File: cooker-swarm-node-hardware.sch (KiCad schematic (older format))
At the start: 18 parts, among them J2 Conn_INPUT, J3 Conn_OUTPUT, Q1 BSS138, Q2 BSS138, U1 nRF52840, U2 MCP6002-xMC

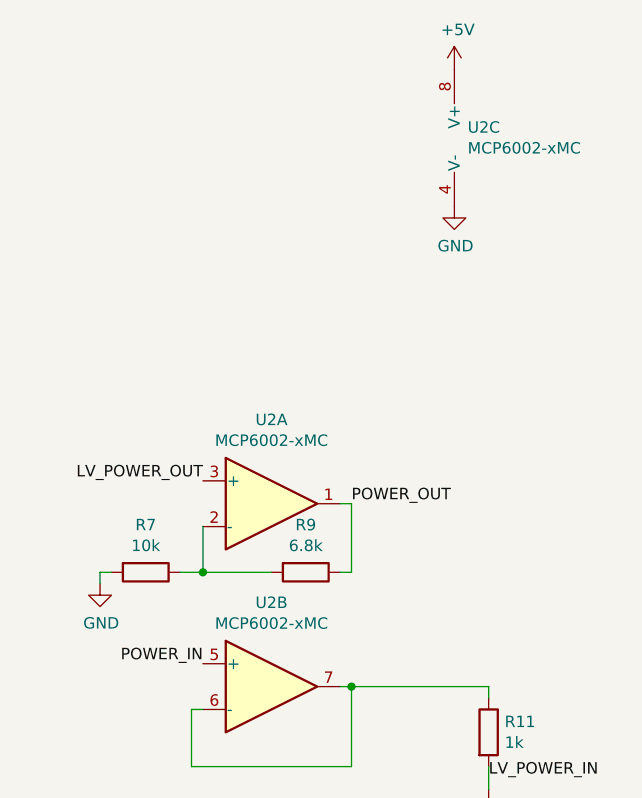
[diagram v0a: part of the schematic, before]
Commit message: use different footprint for operational amplifier
makes soldering more easier
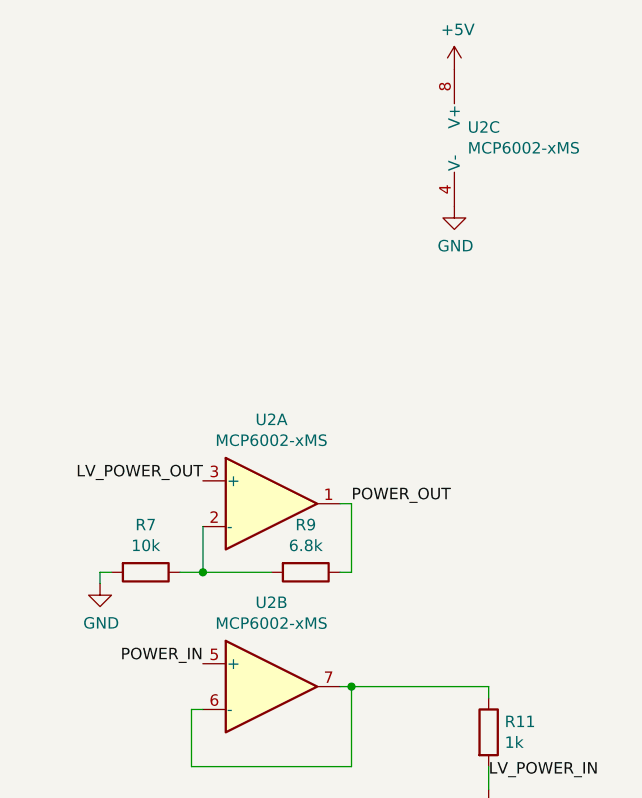
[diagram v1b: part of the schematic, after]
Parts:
- removed U2: MCP6002-xMC, Package_DFN_QFN:DFN-8-1EP_3x2mm_P0.5mm_EP1.75x1.45mm, symbol Amplifier_Operational:MCP6002-xMC
- added U2: MCP6002-xMS, Package_SO:MSOP-8_3x3mm_P0.65mm, symbol Amplifier_Operational:MCP6002-xMS
- J3: footprint Connector_PinHeader_2.54mm:PinHeader_1x10_P2.54mm_Vertical -> Connector_PinSocket_2.54mm:PinSocket_1x10_P2.54mm_Vertical
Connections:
- net +5V: now also U2.8 (V+)
- net GND: now also U2.4 (V-)
- net LV_POWER_OUT: now also U2.3 (+)
- net POWER_IN: now also U2.5 (+)
- net POWER_OUT: now also U2.1
- net at R7.1, R9.2: now also U2.2 (-)
- net at R11.1: now also U2.6 (-), U2.7
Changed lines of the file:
@@
 F 0 "J3" H 2200 1750 50  0000 C CNN
 F 1 "Conn_OUTPUT" H 2000 1650 50  0000 C CNN
-F 2 "Connector_PinHeader_2.54mm:PinHeader_1x10_P2.54mm_Vertical" H 2200 2350 50  0001 C CNN
+F 2 "Connector_PinSocket_2.54mm:PinSocket_1x10_P2.54mm_Vertical" H 2200 2350 50  0001 C CNN
 F 3 "~" H 2200 2350 50  0001 C CNN
 	1    2200 2350
@@
 Wire Wire Line
 	2700 2150 2700 2350
-$Comp
-L Amplifier_Operational:MCP6002-xMC U2
-U 1 1 5DE6A8AB
-P 9700 2650
-F 0 "U2" H 9700 3017 50  0000 C CNN
-F 1 "MCP6002-xMC" H 9700 2926 50  0000 C CNN
-F 2 "Package_DFN_QFN:DFN-8-1EP_3x2mm_P0.5mm_EP1.75x1.45mm" H 9700 2650 50  0001 C CNN
-F 3 "http://ww1.microchip.com/downloads/en/DeviceDoc/21733j.pdf" H 9700 2650 50  0001 C CNN
-	1    9700 2650
-	1    0    0    -1
-$EndComp
-$Comp
-L Amplifier_Operational:MCP6002-xMC U2
-U 2 1 5DE6A930
-P 9700 3450
-F 0 "U2" H 9700 3817 50  0000 C CNN
-F 1 "MCP6002-xMC" H 9700 3726 50  0000 C CNN
-F 2 "Package_DFN_QFN:DFN-8-1EP_3x2mm_P0.5mm_EP1.75x1.45mm" H 9700 3450 50  0001 C CNN
-F 3 "http://ww1.microchip.com/downloads/en/DeviceDoc/21733j.pdf" H 9700 3450 50  0001 C CNN
-	2    9700 3450
-	1    0    0    -1
-$EndComp
-$Comp
-L Amplifier_Operational:MCP6002-xMC U2
-U 3 1 5DE6A988
-P 10600 1050
-F 0 "U2" H 10558 1096 50  0000 L CNN
-F 1 "MCP6002-xMC" H 10558 1005 50  0000 L CNN
-F 2 "Package_DFN_QFN:DFN-8-1EP_3x2mm_P0.5mm_EP1.75x1.45mm" H 10600 1050 50  0001 C CNN
-F 3 "http://ww1.microchip.com/downloads/en/DeviceDoc/21733j.pdf" H 10600 1050 50  0001 C CNN
-	3    10600 1050
-	1    0    0    -1
-$EndComp
 Text Label 9400 3350 2    50   ~ 0
 POWER_IN
@@
 F 3 "" H 10500 750 50  0001 C CNN
 	1    10500 750
-	1    0    0    -1
-$EndComp
-$Comp
-L power:GND #PWR0125
-U 1 1 5DE6ACED
-P 10500 1350
-F 0 "#PWR0125" H 10500 1100 50  0001 C CNN
-F 1 "GND" H 10505 1177 50  0000 C CNN
-F 2 "" H 10500 1350 50  0001 C CNN
-F 3 "" H 10500 1350 50  0001 C CNN
-	1    10500 1350
 	1    0    0    -1
 $EndComp
@@
 NoConn ~ 6900 1950
 NoConn ~ 6900 1750
+$Comp
+L Amplifier_Operational:MCP6002-xMS U2
+U 1 1 5E20C0F7
+P 9700 2650
+F 0 "U2" H 9700 3017 50  0000 C CNN
+F 1 "MCP6002-xMS" H 9700 2926 50  0000 C CNN
+F 2 "Package_SO:MSOP-8_3x3mm_P0.65mm" H 9700 2650 50  0001 C CNN
+F 3 "http://ww1.microchip.com/downloads/en/DeviceDoc/21733j.pdf" H 9700 2650 50  0001 C CNN
+	1    9700 2650
+	1    0    0    -1
+$EndComp
+$Comp
+L Amplifier_Operational:MCP6002-xMS U2
+U 2 1 5E20C183
+P 9700 3450
+F 0 "U2" H 9700 3817 50  0000 C CNN
+F 1 "MCP6002-xMS" H 9700 3726 50  0000 C CNN
+F 2 "" H 9700 3450 50  0001 C CNN
+F 3 "http://ww1.microchip.com/downloads/en/DeviceDoc/21733j.pdf" H 9700 3450 50  0001 C CNN
+	2    9700 3450
+	1    0    0    -1
+$EndComp
+$Comp
+L Amplifier_Operational:MCP6002-xMS U2
+U 3 1 5E20C296
+P 10600 1050
+F 0 "U2" H 10558 1096 50  0000 L CNN
+F 1 "MCP6002-xMS" H 10558 1005 50  0000 L CNN
+F 2 "" H 10600 1050 50  0001 C CNN
+F 3 "http://ww1.microchip.com/downloads/en/DeviceDoc/21733j.pdf" H 10600 1050 50  0001 C CNN
+	3    10600 1050
+	1    0    0    -1
+$EndComp
+$Comp
+L power:GND #PWR0125
+U 1 1 5DE6ACED
+P 10500 1350
+F 0 "#PWR0125" H 10500 1100 50  0001 C CNN
+F 1 "GND" H 10505 1177 50  0000 C CNN
+F 2 "" H 10500 1350 50  0001 C CNN
+F 3 "" H 10500 1350 50  0001 C CNN
+	1    10500 1350
+	1    0    0    -1
+$EndComp
 $EndSCHEMATC

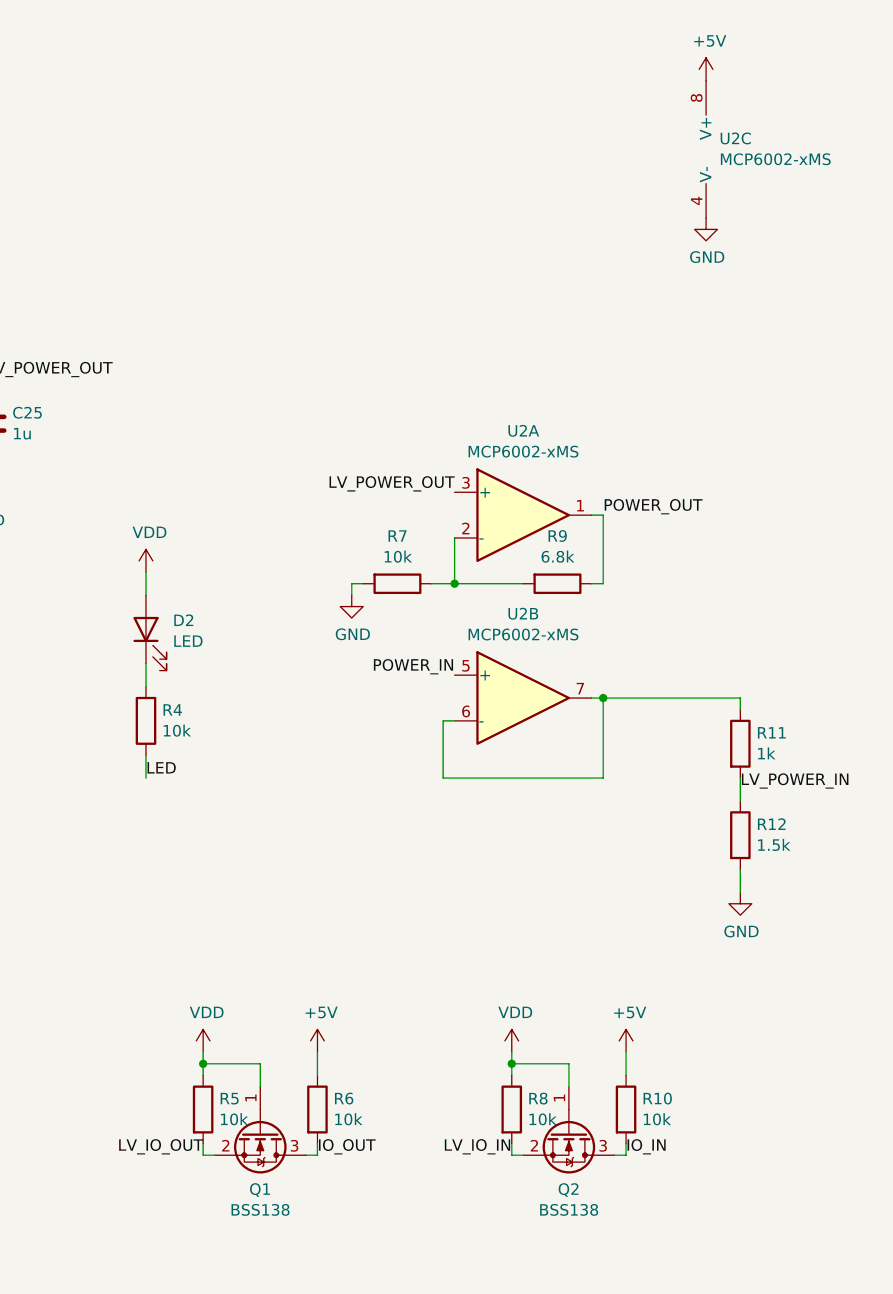
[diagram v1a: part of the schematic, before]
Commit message: use MCP6002 opamp
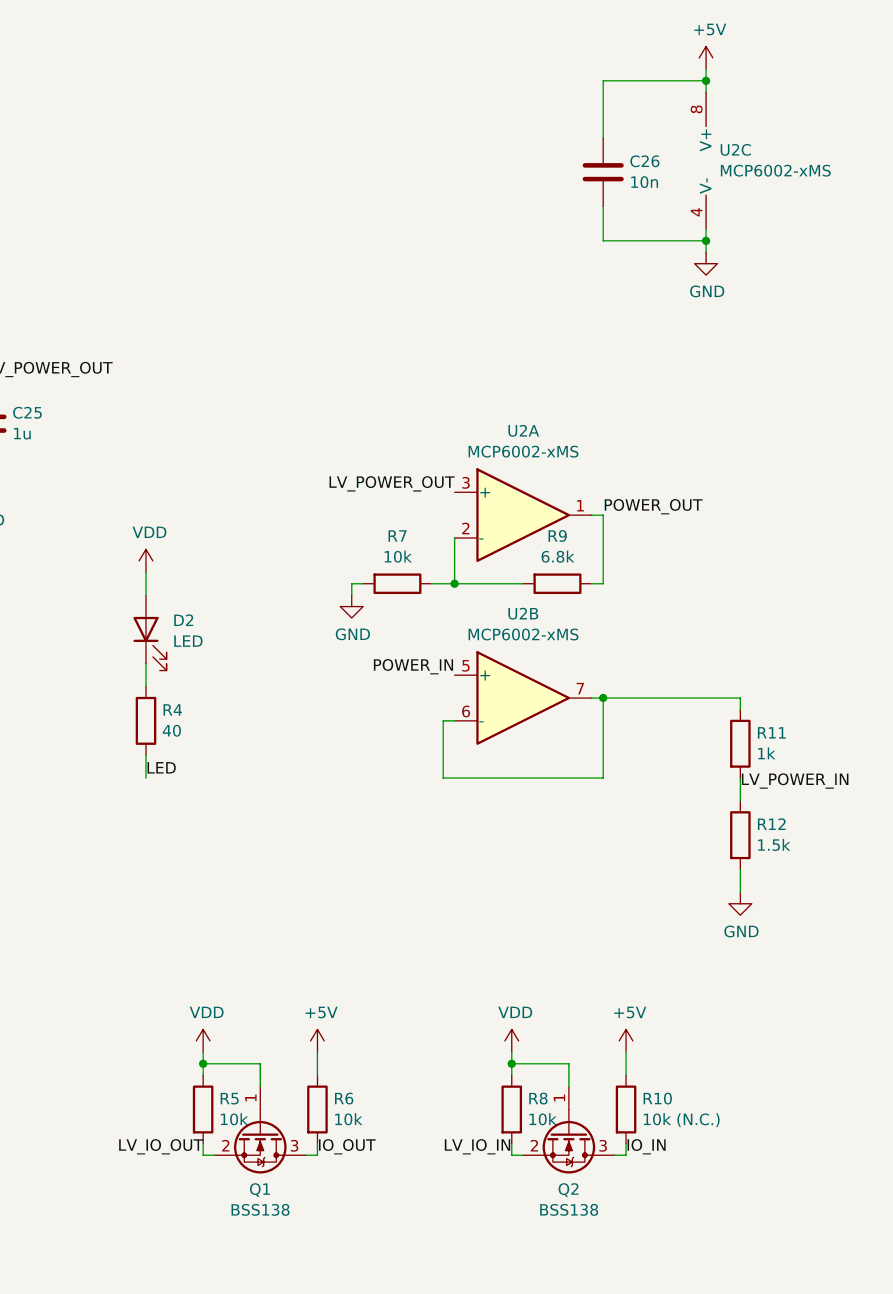
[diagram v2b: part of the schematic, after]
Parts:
- added C26: 10n, Capacitor_SMD:C_0402_1005Metric, symbol Device:C
- D2: footprint LED_SMD:LED_0603_1608Metric -> LED_SMD:LED_1206_3216Metric
- R10: value 10k -> 10k (N.C.)
- R4: value 10k -> 40
- U2: footprint (none) -> Package_SO:MSOP-8_3x3mm_P0.65mm
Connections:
- net +5V: now also C26.1
- net GND: now also C26.2
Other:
- moved on the sheet: U2C
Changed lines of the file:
@@
 L power:+5V #PWR0124
 U 1 1 5DE6ACD2
-P 10500 750
-F 0 "#PWR0124" H 10500 600 50  0001 C CNN
-F 1 "+5V" H 10515 923 50  0000 C CNN
-F 2 "" H 10500 750 50  0001 C CNN
-F 3 "" H 10500 750 50  0001 C CNN
-	1    10500 750
+P 10500 700
+F 0 "#PWR0124" H 10500 550 50  0001 C CNN
+F 1 "+5V" H 10515 873 50  0000 C CNN
+F 2 "" H 10500 700 50  0001 C CNN
+F 3 "" H 10500 700 50  0001 C CNN
+	1    10500 700
 	1    0    0    -1
 $EndComp
@@
 P 10150 5250
 F 0 "R10" H 10220 5296 50  0000 L CNN
-F 1 "10k" H 10220 5205 50  0000 L CNN
+F 1 "10k (N.C.)" H 10220 5205 50  0000 L CNN
 F 2 "Resistor_SMD:R_0402_1005Metric" V 10080 5250 50  0001 C CNN
 F 3 "~" H 10150 5250 50  0001 C CNN
@@
 F 0 "D2" V 8088 3033 50  0000 R CNN
 F 1 "LED" V 7997 3033 50  0000 R CNN
-F 2 "LED_SMD:LED_0603_1608Metric" H 8050 3150 50  0001 C CNN
+F 2 "LED_SMD:LED_1206_3216Metric" H 8050 3150 50  0001 C CNN
 F 3 "~" H 8050 3150 50  0001 C CNN
 	1    8050 3150
@@
 P 8050 3550
 F 0 "R4" H 7980 3504 50  0000 R CNN
-F 1 "10k" H 7980 3595 50  0000 R CNN
+F 1 "40" H 7980 3595 50  0000 R CNN
 F 2 "Resistor_SMD:R_0402_1005Metric" V 7980 3550 50  0001 C CNN
 F 3 "~" H 8050 3550 50  0001 C CNN
@@
 F 0 "U2" H 9700 3817 50  0000 C CNN
 F 1 "MCP6002-xMS" H 9700 3726 50  0000 C CNN
-F 2 "" H 9700 3450 50  0001 C CNN
+F 2 "Package_SO:MSOP-8_3x3mm_P0.65mm" H 9700 3450 50  0001 C CNN
 F 3 "http://ww1.microchip.com/downloads/en/DeviceDoc/21733j.pdf" H 9700 3450 50  0001 C CNN
 	2    9700 3450
@@
 L Amplifier_Operational:MCP6002-xMS U2
 U 3 1 5E20C296
-P 10600 1050
-F 0 "U2" H 10558 1096 50  0000 L CNN
-F 1 "MCP6002-xMS" H 10558 1005 50  0000 L CNN
-F 2 "" H 10600 1050 50  0001 C CNN
-F 3 "http://ww1.microchip.com/downloads/en/DeviceDoc/21733j.pdf" H 10600 1050 50  0001 C CNN
-	3    10600 1050
+P 10600 1100
+F 0 "U2" H 10558 1146 50  0000 L CNN
+F 1 "MCP6002-xMS" H 10558 1055 50  0000 L CNN
+F 2 "Package_SO:MSOP-8_3x3mm_P0.65mm" H 10600 1100 50  0001 C CNN
+F 3 "http://ww1.microchip.com/downloads/en/DeviceDoc/21733j.pdf" H 10600 1100 50  0001 C CNN
+	3    10600 1100
 	1    0    0    -1
 $EndComp
@@
 L power:GND #PWR0125
 U 1 1 5DE6ACED
-P 10500 1350
-F 0 "#PWR0125" H 10500 1100 50  0001 C CNN
-F 1 "GND" H 10505 1177 50  0000 C CNN
-F 2 "" H 10500 1350 50  0001 C CNN
-F 3 "" H 10500 1350 50  0001 C CNN
-	1    10500 1350
-	1    0    0    -1
-$EndComp
+P 10500 1500
+F 0 "#PWR0125" H 10500 1250 50  0001 C CNN
+F 1 "GND" H 10505 1327 50  0000 C CNN
+F 2 "" H 10500 1500 50  0001 C CNN
+F 3 "" H 10500 1500 50  0001 C CNN
+	1    10500 1500
+	1    0    0    -1
+$EndComp
+$Comp
+L Device:C C26
+U 1 1 6167308B
+P 10050 1150
+F 0 "C26" H 10165 1196 50  0000 L CNN
+F 1 "10n" H 10165 1105 50  0000 L CNN
+F 2 "Capacitor_SMD:C_0402_1005Metric" H 10088 1000 50  0001 C CNN
+F 3 "~" H 10050 1150 50  0001 C CNN
+	1    10050 1150
+	1    0    0    -1
+$EndComp
+Wire Wire Line
+	10500 1450 10050 1450
+Wire Wire Line
+	10050 1450 10050 1300
+Wire Wire Line
+	10050 1000 10050 750
+Wire Wire Line
+	10050 750  10500 750
+Wire Wire Line
+	10500 750  10500 800
+Wire Wire Line
+	10500 750  10500 700
+Connection ~ 10500 750
+Wire Wire Line
+	10500 1400 10500 1450
+Wire Wire Line
+	10500 1500 10500 1450
+Connection ~ 10500 1450
 $EndSCHEMATC
